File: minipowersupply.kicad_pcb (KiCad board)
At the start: 2 copper layers, 147.4 x 37.3 mm, 107 parts, among them J1 Conn_01x01_Female, J10 Conn_01x03_Female, J11 Conn_01x08_Female, J12 Conn_01x03_Female, J13 Conn_01x08_Female, J14 Conn_01x03_Female, J15 Conn_01x08_Female, J16 Conn_01x02_Female, J17 Conn_01x08_Female, J18 Conn_01x02_Female, J2 Conn_01x03_Male, J3 Conn_01x01_Female, J4 Conn_01x01_Female, J5 Conn_01x03_Male, J6 Conn_01x01_Female, J7 Conn_01x01_Female, J8 Conn_01x03_Male, J9 Conn_01x01_Female, Q1 BC817, U1 ACS70331EOLCTR-2P5U3, U10 ACS70331EOLCTR-2P5U3, U2 ACS70331EOLCTR-2P5U3, U3 ACS70331EOLCTR-2P5U3, U4 CD74HC4067SM, U5 ACS70331EOLCTR-2P5U3, U6 LM7805_TO220, U7 LM317L_TO92, U8 LM337L_TO92, U9 LM358

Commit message: new board with SMD
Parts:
- removed the C10 at (169.0, 123.4)
- removed the C11 at (173.0, 123.4)
- removed the C17 at (165.0, 126.0)
- removed the C18 at (182.4, 133.7)
- removed the C19 at (182.4, 131.2)
- removed the C20 at (186.4, 131.2)
- removed the C21 at (102.4, 57.1)
- removed the C22 at (105.4, 57.1)
- removed the C23 at (115.3, 57.1)
- removed the C26 at (125.2, 57.7)
- removed the C27 at (121.9, 57.7)
- removed C41, C42: 0.1uF, Capacitor_SMD:C_0603_1608Metric
- removed J10, J12, J14: Conn_01x03_Female, Connector_PinHeader_2.54mm:PinHeader_1x03_P2.54mm_Vertical
- removed J11, J13, J15, J17: Conn_01x08_Female, Connector_PinHeader_2.54mm:PinHeader_1x08_P2.54mm_Vertical
- removed the J2 at (101.5, 89.2)
- removed the J5 at (126.2, 89.2)
- removed the J8 at (116.4, 89.2)
- removed the J9 at (112.8, 116.3)
- removed the U5 at (118.2, 102.1)
- removed the U9 at (168.6, 111.3)
- added C15: 0.1uF, Capacitor_SMD:C_0603_1608Metric, F.Cu at (300.6, 79.4)
- added C16: 0.1uF, Capacitor_SMD:C_0603_1608Metric, F.Cu at (300.6, 81.9)
- added C32: 0.1uF, Capacitor_SMD:C_0603_1608Metric, F.Cu at (334.4, 85.8)
- added C33: 0.1uF, Capacitor_SMD:C_0603_1608Metric, F.Cu at (339.3, 79.4)
- added C34: 0.1uF, Capacitor_SMD:C_0603_1608Metric, F.Cu at (338.4, 85.8)
- added J6: Conn_01x01_Female, Connector_PinHeader_2.54mm:PinHeader_1x01_P2.54mm_Vertical, F.Cu at (263.9, 117.3)
- added J7: Conn_01x01_Female, Connector_PinHeader_2.54mm:PinHeader_1x01_P2.54mm_Vertical, F.Cu at (300.9, 93.8)
- added U11: ACS70331EOLCTR-2P5U3, ACS70331EOLCTR-2P5U3:SOIC127P600X175-8N, F.Cu at (333.1, 81.4)
- added U4: LM358, Package_TO_SOT_SMD:SOT-223-8, F.Cu at (293.0, 95.6)
- added U6: LM358, Package_TO_SOT_SMD:SOT-223-8, F.Cu at (293.0, 82.3)
- R19: value 10k -> 20k
- R7: value 20k -> 10k
- moved R20 255.3 mm to (339.3, 81.9)
- moved R19 246.5 mm to (330.4, 85.8)
- moved R2 211.2 mm to (319.7, 81.9), turned to 0 degrees
- moved U1 207.0 mm to (313.5, 81.4), turned to 0 degrees
- moved R1 206.1 mm to (310.8, 85.8)
- moved R4 202.0 mm to (338.0, 94.2), turned to 0 degrees
- moved U2 197.2 mm to (331.8, 93.7), turned to 0 degrees
- moved R3 197.2 mm to (329.1, 98.2)
- moved R6 190.7 mm to (318.4, 95.2), turned to 0 degrees
- moved R7 186.7 mm to (300.6, 86.9)
- moved R5 186.0 mm to (309.5, 99.2)
- moved U3 185.8 mm to (312.2, 94.7), turned to 0 degrees
- moved R8 182.7 mm to (300.6, 84.4), turned to 0 degrees
- moved C5 147.2 mm to (338.0, 91.7)
- moved C2 143.5 mm to (319.7, 79.4)
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- renumbered C12 to C10, C13 to C11, C14 to C12, C15 to C13, C16 to C14, C24 to C17, C25 to C18, C28 to C19, C29 to C20, C30 to C21, C31 to C22, C32 to C23, C33 to C24, C34 to C25, C35 to C26, C36 to C27, C40 to C28, C37 to C29, C38 to C30, C39 to C31, J3 to J2, J4 to J3, J6 to J4, J7 to J5, J16 to J8, J18 to J9, R18 to R16, R16 to R17, R17 to R18, U4 to U5, U6 to U7, U7 to U8, U8 to U9
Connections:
- net +5VA renamed /Clock and TTL/V5Out
- net / Measure and Mux/3v3 renamed 3V3
- net / Measure and Mux/A0 renamed /Filter and Mux/A0
- net / Measure and Mux/A1 renamed /Filter and Mux/A1
- net / Measure and Mux/A2 renamed /Filter and Mux/A2
- net / Measure and Mux/A3 renamed /Filter and Mux/A3
- net / Measure and Mux/Aout renamed /Filter and Mux/Aout
- net / Measure and Mux/Curent and Volt4/Isense renamed /Filter and Mux/Curent and Volt4/Isense
- net / Measure and Mux/Curent and Volt4/Out V renamed /Filter and Mux/Curent and Volt4/Vout
- net / Measure and Mux/Curent and Volt4/Vsense renamed /Filter and Mux/Curent and Volt4/Vsense
- net / Measure and Mux/Curent and Volt5/Isense renamed /Filter and Mux/Curent and Volt5/Isense
- net / Measure and Mux/Curent and Volt5/Out V renamed /Filter and Mux/Curent and Volt5/Vout
- net / Measure and Mux/Curent and Volt6/Isense renamed /Filter and Mux/Curent and Volt6/Isense
- net / Measure and Mux/Curent and Volt6/Out V renamed /Filter and Mux/Curent and Volt6/Vout
- net / Measure and Mux/Curent and Volt6/Vsense renamed /Filter and Mux/Curent and Volt6/Vsense
- net / Measure and Mux/Curent and Volt7/Isense renamed /Filter and Mux/Curent and Volt7/Isense
- net / Measure and Mux/Curent and Volt7/Out V renamed /Filter and Mux/Curent and Volt7/Vout
- net / Measure and Mux/EN renamed /Filter and Mux/EN
- net / Measure and Mux/V5+ renamed V5
- A1 pad 20: unconnected-(A1-Pad20) -> /Clock and TTL/CK_Out
- A1 pad 29: / Measure and Mux/GND -> GNDREF
- A1 pad 30: / Measure and Mux/Vunreg+ -> /Unregulated Power/V+
- A1 pad 4: / Measure and Mux/GND -> GNDREF
- C1 pad 1: / Measure and Mux/GND -> GNDREF
- C10 pad 1: / Measure and Mux/GND -> GNDREF
- C11 pad 1: / Measure and Mux/GND -> GNDREF
- C12 pad 1: / Measure and Mux/GND -> GNDREF
- C13 pad 1: / Measure and Mux/GND -> GNDREF
- C14 pad 1: / Measure and Mux/GND -> GNDREF
- C14 pad 2: / Measure and Mux/Curent and Volt8/Out V -> /Filter and Mux/Curent and Volt8/Vout
- C17 pad 1: /Unregulated Power/GND -> GNDREF
- C18 pad 2: /Unregulated Power/GND -> GNDREF
- C19 pad 1: Net-(C28-Pad1) -> /Unregulated Power/V+
- C19 pad 2: /Clock and TTL/GND_0 -> GNDREF
- C2 pad 2: / Measure and Mux/GND -> GNDREF
- C20 pad 2: /Clock and TTL/GND_0 -> GNDREF
- C21 pad 1: /Clock and TTL/CK -> /Clock and TTL/CK_Out
- C21 pad 2: /Clock and TTL/GND_0 -> GNDREF
- C22 pad 1: Net-(C31-Pad1) -> /Unregulated Power/V+
- C22 pad 2: /DualAdj/GND -> GNDREF
- C23 pad 1: Net-(C32-Pad1) -> /DualAdj/Vreg+
- C23 pad 2: /DualAdj/GND -> GNDREF
- C24 pad 1: Net-(C33-Pad1) -> /Unregulated Power/V-
- C24 pad 2: /DualAdj/GND -> Net-(C24-Pad2)
- C25 pad 1: /DualAdj/GND -> Net-(C24-Pad2)
- C25 pad 2: Net-(C34-Pad2) -> /DualAdj/Vreg-
- C26 pad 1: / Measure and Mux/Curent and Volt7/Vsense -> /Filter and Mux/Curent and Volt5/Vsense
- C26 pad 2: / Measure and Mux/GND -> GNDREF
- C27 pad 1: / Measure and Mux/Unity Inverter1/Ainv -> /Filter and Mux/Unity Inverter/Ainv
- C27 pad 2: / Measure and Mux/GND -> GNDREF
- C28 pad 1: / Measure and Mux/GND -> GNDREF
- C29 pad 1: / Measure and Mux/GND -> GNDREF
- C3 pad 1: / Measure and Mux/Curent and Volt5/Vsense -> /Filter and Mux/Curent and Volt5/Vsense
- C3 pad 2: / Measure and Mux/GND -> GNDREF
- C30 pad 2: / Measure and Mux/GND -> GNDREF
- C31 pad 2: / Measure and Mux/GND -> GNDREF
- C4 pad 1: / Measure and Mux/GND -> GNDREF
- C5 pad 2: / Measure and Mux/GND -> GNDREF
- C6 pad 2: / Measure and Mux/GND -> GNDREF
- C7 pad 1: / Measure and Mux/GND -> GNDREF
- C8 pad 2: / Measure and Mux/GND -> GNDREF
- C9 pad 1: / Measure and Mux/Curent and Volt7/Vsense -> /Filter and Mux/Curent and Volt7/Vsense
- C9 pad 2: / Measure and Mux/GND -> GNDREF
- D1 pad 1: Net-(D1-Pad1) -> /Clock and TTL/HalfSineIn
- D6 pad 1: Net-(D1-Pad1) -> /Clock and TTL/HalfSineIn
- D7 pad 1: /Clock and TTL/GND_0 -> GNDREF
- D8 pad 2: /Clock and TTL/GND_0 -> GNDREF
- D9 pad 1: / Measure and Mux/GND -> GNDREF
- DS1 pad 1: / Measure and Mux/GND -> GNDREF
- DS1 pad 30: / Measure and Mux/GND -> GNDREF
- J5 pad 1: / Measure and Mux/Curent and Volt8/Out V -> /Filter and Mux/Curent and Volt8/Vout
- J8 pad 1: /DualAdj/GND -> GNDREF
- J9 pad 1: /DualAdj/GND -> Net-(C24-Pad2)
- Q1 pad 2: /Clock and TTL/GND_0 -> GNDREF
- Q1 pad 3: /Clock and TTL/CK -> /Clock and TTL/CK_Out
- R1 pad 2: / Measure and Mux/Curent and Volt5/Vsense -> /Filter and Mux/Curent and Volt5/Vsense
- R10 pad 2: Net-(J15-Pad4) -> /Clock and TTL/HalfSineIn
- R11 pad 2: /Clock and TTL/GND_0 -> GNDREF
- R12 pad 1: Net-(C32-Pad1) -> /DualAdj/Vreg+
- R13 pad 1: Net-(C34-Pad2) -> /DualAdj/Vreg-
- R14 pad 2: / Measure and Mux/Unity Inverter1/Ainv -> /Filter and Mux/Unity Inverter/Ainv
- R15 pad 1: / Measure and Mux/Curent and Volt7/Vsense -> /Filter and Mux/Curent and Volt5/Vsense
- R18 pad 2: / Measure and Mux/GND -> GNDREF
- R19 pad 1: Net-(R19-Pad1) -> /Filter and Mux/Curent and Volt8/Vout
- R19 pad 2: / Measure and Mux/Unity Inverter/Ainv -> /Filter and Mux/Curent and Volt8/Vsense
- R2 pad 1: / Measure and Mux/Curent and Volt5/Vsense -> /Filter and Mux/Curent and Volt5/Vsense
- R2 pad 2: / Measure and Mux/GND -> GNDREF
- R20 pad 1: / Measure and Mux/Curent and Volt5/Vsense -> /Filter and Mux/Curent and Volt8/Vsense
- R20 pad 2: Net-(R19-Pad1) -> GNDREF
- R4 pad 2: / Measure and Mux/GND -> GNDREF
- R5 pad 2: / Measure and Mux/Curent and Volt7/Vsense -> /Filter and Mux/Curent and Volt7/Vsense
- R6 pad 1: / Measure and Mux/Curent and Volt7/Vsense -> /Filter and Mux/Curent and Volt7/Vsense
- R6 pad 2: / Measure and Mux/GND -> GNDREF
- R7 pad 1: / Measure and Mux/Curent and Volt8/Out V -> Net-(R7-Pad1)
- R7 pad 2: / Measure and Mux/Curent and Volt8/Vsense -> /Filter and Mux/Unity Inverter1/Ainv
- R8 pad 1: / Measure and Mux/Curent and Volt8/Vsense -> /Filter and Mux/Curent and Volt7/Vsense
- R8 pad 2: / Measure and Mux/GND -> Net-(R7-Pad1)
- R9 pad 2: /Clock and TTL/CK -> /Clock and TTL/CK_Out
- TP3 pad 1: /Unregulated Power/GND -> GNDREF
- TR1 pad 4: /Unregulated Power/GND -> GNDREF
- TR1 pad 5: /Unregulated Power/GND -> GNDREF
- U1 pad 3: / Measure and Mux/Vunreg- -> /Unregulated Power/V-
- U1 pad 4: / Measure and Mux/Vunreg- -> /Unregulated Power/V-
- U1 pad 5: / Measure and Mux/GND -> GNDREF
- U10 pad 3: / Measure and Mux/Vunreg+ -> /Unregulated Power/V+
- U10 pad 4: / Measure and Mux/Vunreg+ -> /Unregulated Power/V+
- U10 pad 5: / Measure and Mux/GND -> GNDREF
- U2 pad 3: / Measure and Mux/Curent and Volt6/Vin -> /DualAdj/Vreg+
- U2 pad 4: / Measure and Mux/Curent and Volt6/Vin -> /DualAdj/Vreg+
- U2 pad 5: / Measure and Mux/GND -> GNDREF
- U3 pad 3: / Measure and Mux/Curent and Volt7/Vin -> /DualAdj/Vreg-
- U3 pad 4: / Measure and Mux/Curent and Volt7/Vin -> /DualAdj/Vreg-
- U3 pad 5: / Measure and Mux/GND -> GNDREF
- U5 pad 12: / Measure and Mux/GND -> GNDREF
- U5 pad 22: / Measure and Mux/Curent and Volt8/Isense -> /Filter and Mux/Curent and Volt8/Isense
- U5 pad 23: / Measure and Mux/Curent and Volt8/Vsense -> /Filter and Mux/Curent and Volt8/Vsense
- U5 pad 3: / Measure and Mux/Unity Inverter1/Ainv -> /Filter and Mux/Unity Inverter1/Ainv
- U5 pad 7: / Measure and Mux/Unity Inverter/Ainv -> /Filter and Mux/Unity Inverter/Ainv
- U7 pad 1: Net-(C28-Pad1) -> /Unregulated Power/V+
- U7 pad 2: /Clock and TTL/GND_0 -> GNDREF
- U8 pad 2: Net-(C32-Pad1) -> /DualAdj/Vreg+
- U8 pad 3: Net-(C31-Pad1) -> /Unregulated Power/V+
- U9 pad 2: Net-(C34-Pad2) -> /DualAdj/Vreg-
- U9 pad 3: Net-(C33-Pad1) -> /Unregulated Power/V-
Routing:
- net /Unregulated Power/V-: track 57.8 -> 21.1 mm
- net /Unregulated Power/V+: track 108.5 -> 73.3 mm
- net /Clock and TTL/CK: track 27.1 -> 0.00 mm
- net /Clock and TTL/V5Out: track 25.6 -> 0.00 mm, vias 1 -> 0
- net Net-(C32-Pad1): track 23.3 -> 0.00 mm
- net Net-(C34-Pad2): track 22.0 -> 0.00 mm
- net Net-(C23-Pad1): track 20.6 -> 0.00 mm
- net Net-(C26-Pad2): track 19.7 -> 0.00 mm
- net Net-(C33-Pad1): track 15.9 -> 0.00 mm
- net Net-(D1-Pad1): track 14.8 -> 0.00 mm, vias 1 -> 0
- net Net-(D7-Pad2): track 13.7 -> 0.00 mm
- net Net-(J11-Pad8): track 11.9 -> 0.00 mm
- net Net-(C27-Pad1): track 11.8 -> 0.00 mm
- net Net-(J9-Pad2): track 11.5 -> 0.00 mm
- net Net-(J8-Pad2): track 8.76 -> 0.00 mm
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- added copper zone on B.Cu, net GNDREF
- added copper zone on F.Cu, net GNDREF
- removed copper zone on B.Cu, net /Clock and TTL/GND_0
- removed copper zone on F.Cu, net /Clock and TTL/GND_0
- removed copper zone on B.Cu, net /DualAdj/GND
- removed copper zone on F.Cu, net /DualAdj/GND
- removed copper zone on B.Cu, net /Unregulated Power/GND
- removed copper zone on F.Cu, net /Unregulated Power/GND
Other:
- board size 147.4 x 37.3 mm -> 126.5 x 129 mm

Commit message: New single board with all SMD in progress
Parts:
- removed U4: LM358, Package_TO_SOT_SMD:SOT-223-8
- C19, C20, U7: moved to F.Cu
- C21, D7, D8, Q1, R10, R11, R12, R15, R7: moved to B.Cu
- C23, C25: footprint Capacitor_SMD:C_1206_3216Metric -> Capacitor_SMD:C_0603_1608Metric
- moved U11 168.0 mm to (165.2, 75.0), turned to -90 degrees
- moved U2 166.7 mm to (165.2, 87.0), turned to -90 degrees
- moved R20 158.2 mm to (181.2, 75.3), turned to 180 degrees
- moved R4 156.6 mm to (181.5, 88.1), turned to 180 degrees
- moved R19 147.1 mm to (183.9, 73.2), turned to -90 degrees
- moved U3 147.0 mm to (165.2, 99.0), turned to -90 degrees
- moved R3 145.7 mm to (183.9, 86.2), turned to -90 degrees
- moved C2 144.7 mm to (175.8, 94.6), turned to 90 degrees
- moved U1 141.8 mm to (172.2, 93.0), turned to -90 degrees
- moved C1 141.7 mm to (173.6, 97.4), turned to 180 degrees
- moved R2 139.2 mm to (181.1, 94.5), turned to 180 degrees
- moved R6 137.4 mm to (181.1, 100.9), turned to 180 degrees
- moved C3 134.8 mm to (184.4, 95.0)
- moved C27 129.2 mm to (167.7, 108.7), turned to -90 degrees
- moved R1 127.4 mm to (183.6, 92.7), turned to -90 degrees
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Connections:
- U6 pad 1: (no net) -> /Filter and Mux/Unity Inverter1/Ainv
- U6 pad 2: (no net) -> Net-(R7-Pad1)
- U6 pad 3: (no net) -> GNDREF
- U6 pad 4: (no net) -> /Unregulated Power/V-
- U6 pad 6: Net-(R7-Pad1) -> Net-(R14-Pad1)
- U6 pad 7: /Filter and Mux/Unity Inverter1/Ainv -> /Filter and Mux/Unity Inverter/Ainv
- U6 pad 8: (no net) -> /Unregulated Power/V+
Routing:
- net /Unregulated Power/V+: track 73.3 -> 115.4 mm
- net Net-(R7-Pad1): vias 0 -> 1
- net Net-(R14-Pad1): vias 0 -> 1
- net /Filter and Mux/Unity Inverter1/Ainv: vias 0 -> 1
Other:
- board size 126.5 x 129 mm -> 102.2 x 63 mm
- board text added: "Safety Cutouts"
- board text added: "VUnreg"
- board text added: "VUnreg-"
- board text added: "Vreg+"

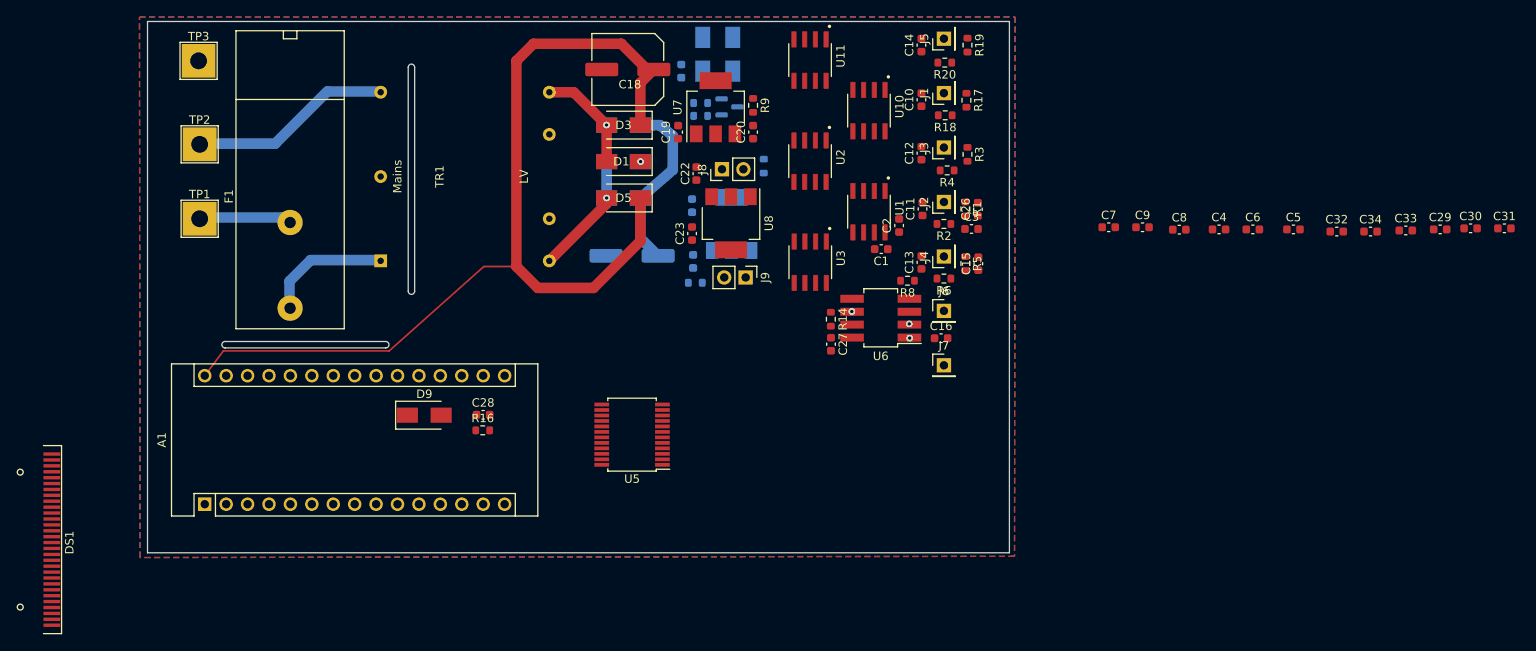
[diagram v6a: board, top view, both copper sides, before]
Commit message: Updated improved board for all SMD
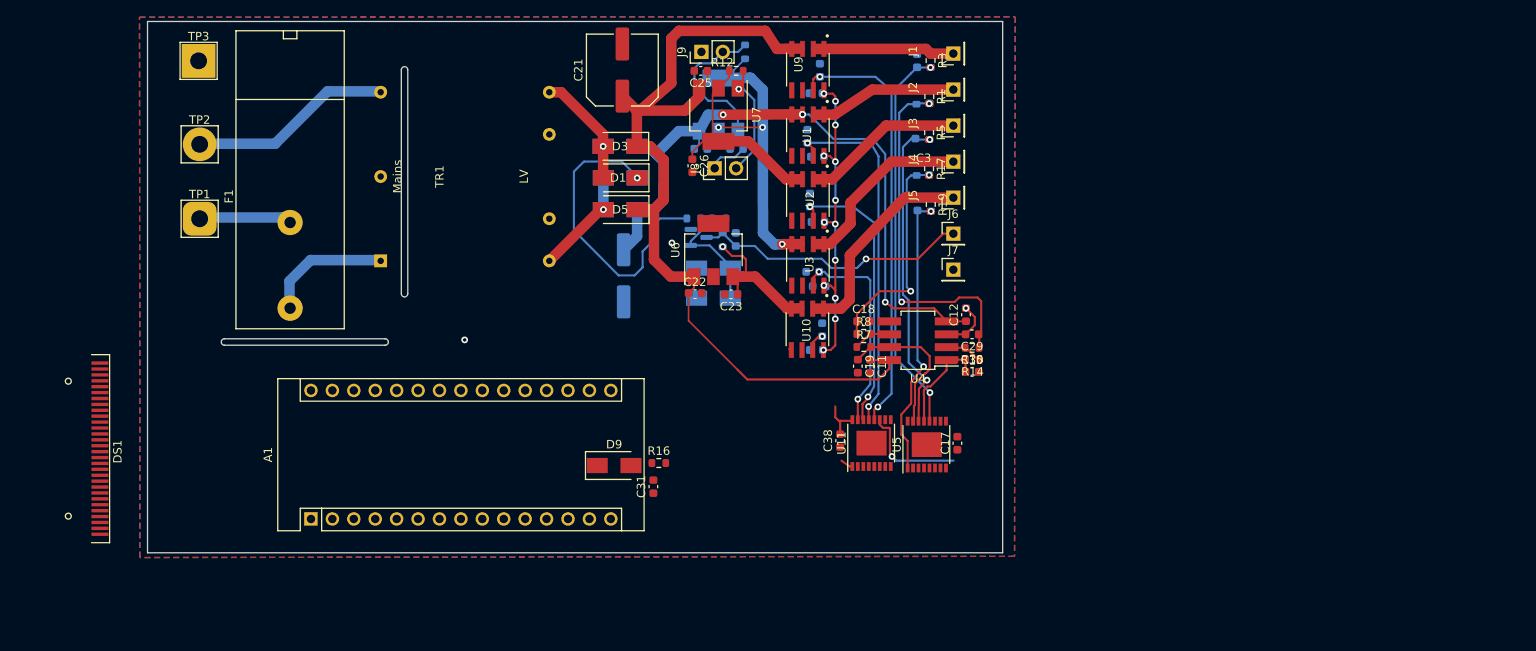
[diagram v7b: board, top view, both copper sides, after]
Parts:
- removed C14, C15, C16, C34: 0.1uF, Capacitor_SMD:C_0603_1608Metric
- added C35: 0.1uF, Capacitor_SMD:C_0603_1608Metric, B.Cu at (166.6, 107.0)
- added C36: 0.1uF, Capacitor_SMD:C_0603_1608Metric, B.Cu at (165.9, 109.4)
- added C38: 0.1uF, Capacitor_SMD:C_0603_1608Metric, F.Cu at (168.8, 120.2)
- added U4: LM358, Package_TO_SOT_SMD:SOT-223-8, F.Cu at (178.0, 108.3)
- A1: value Arduino_Nano_v2.x -> Arduino_Nano_v3.x
- C1, C10, C13, C2, C27, C3, C32, C33, C4, C5, C6, C7, C8, C9, R18, R2, R20, R4, R6, R9: moved to B.Cu
- C17: value 150uF -> 0.1uF; footprint Capacitor_SMD:C_Elec_8x6.2 -> Capacitor_SMD:C_0603_1608Metric; moved to F.Cu
- C18: value 150uF -> 0.1uF; footprint Capacitor_SMD:C_Elec_8x6.2 -> Capacitor_SMD:C_0603_1608Metric
- C20: value 0.1uF -> 150uF; footprint Capacitor_SMD:C_0603_1608Metric -> Capacitor_SMD:C_Elec_8x6.2; moved to B.Cu
- C21: value 0.1uF -> 150uF; footprint Capacitor_SMD:C_0603_1608Metric -> Capacitor_SMD:C_Elec_8x6.2; moved to F.Cu
- C23: value 1uF -> 0.1uF
- C25: value 1uF -> 0.1uF; moved to F.Cu
- C26: value 0.1uF -> 1uF
- C28: value 0.1uF -> 1uF; moved to B.Cu
- R12, R15, R7: moved to F.Cu
- U11: value ACS70331EOLCTR-2P5U3 -> 74HC4051; footprint ACS70331EOLCTR-2P5U3:SOIC127P600X175-8N -> Package_SO:TSSOP-16-1EP_4.4x5mm_P0.65mm
- U5: value CD74HC4067SM -> 74HC4051; footprint Package_SO:SSOP-24_5.3x8.2mm_P0.65mm -> Package_SO:TSSOP-16-1EP_4.4x5mm_P0.65mm
- U6: value LM358 -> LM7805_TO220; footprint Package_TO_SOT_SMD:SOT-223-8 -> Package_TO_SOT_SMD:SOT-223-3_TabPin2
- U7: value LM7805_TO220 -> LM317L_TO92
- U8: value LM317L_TO92 -> LM337L_TO92; moved to B.Cu
- U9: value LM337L_TO92 -> ACS70331EOLCTR-2P5U3; footprint Package_TO_SOT_SMD:SOT-223-3_TabPin2 -> ACS70331EOLCTR-2P5U3:SOIC127P600X175-8N; moved to F.Cu
- moved C31 105.5 mm to (146.6, 125.6), turned to 90 degrees
- moved C33 71.8 mm to (165.9, 79.0), turned to 180 degrees
- moved C32 64.2 mm to (166.4, 76.2), turned to -90 degrees
- moved C30 61.5 mm to (184.4, 112.0)
- moved C29 56.9 mm to (184.4, 107.5), turned to 180 degrees
- moved C5 56.4 mm to (166.2, 94.2), turned to 180 degrees
- moved C4 48.6 mm to (165.2, 91.6), turned to -90 degrees
- moved U11 46.0 mm to (172.5, 120.4), turned to 90 degrees
- moved C6 44.6 mm to (177.9, 75.1), turned to 90 degrees
- moved C17 44.5 mm to (182.7, 120.5), turned to 90 degrees
- moved C28 43.6 mm to (156.5, 85.5), turned to 180 degrees
- moved C8 43.2 mm to (166.3, 101.8), turned to 180 degrees
- moved C18 40.9 mm to (171.5, 106.0), turned to 0 degrees
- moved C7 35.5 mm to (165.5, 100.1)
- moved C19 35.0 mm to (170.9, 111.3), turned to -90 degrees
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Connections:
- A1 pad 10: /Filter and Mux/A3 -> unconnected-(A1-Pad10)
- A1 pad 11: /Filter and Mux/A2 -> /I V Sensor and Mux/A2
- A1 pad 12: /Filter and Mux/A1 -> /I V Sensor and Mux/A1
- A1 pad 13: /Filter and Mux/A0 -> /I V Sensor and Mux/A0
- A1 pad 14: /Filter and Mux/EN -> unconnected-(A1-Pad14)
- A1 pad 20: /Clock and TTL/CK_Out -> /I V Sensor and Mux/Amp
- A1 pad 21: unconnected-(A1-Pad21) -> /Clock and TTL/CK_Out
- A1 pad 30: /Unregulated Power/V+ -> /Clock and TTL/VUnreg+
- C1 pad 2: /Filter and Mux/Curent and Volt5/Isense -> /I V Sensor and Mux/Curent and Volt5/Isense
- C10 pad 1: GNDREF -> /I V Sensor and Mux/Unity Inverter1/Ain
- C10 pad 2: /Filter and Mux/Curent and Volt4/Vout -> GNDREF
- C11 pad 1: GNDREF -> /Clock and TTL/VUnreg+
- C11 pad 2: /Filter and Mux/Curent and Volt5/Vout -> GNDREF
- C12 pad 1: GNDREF -> /DualAdj/VUnreg-
- C12 pad 2: /Filter and Mux/Curent and Volt6/Vout -> GNDREF
- C13 pad 1: GNDREF -> /I V Sensor and Mux/V5+i
- C13 pad 2: /Filter and Mux/Curent and Volt7/Vout -> GNDREF
- C17 pad 2: /Unregulated Power/V- -> V5
- C18 pad 1: /Unregulated Power/V+ -> /I V Sensor and Mux/Unity Inverter1/Ain
- C19 pad 1: /Unregulated Power/V+ -> /I V Sensor and Mux/VA-i
- C20 pad 1: /Clock and TTL/V5Out -> GNDREF
- C20 pad 2: GNDREF -> /DualAdj/VUnreg-
- C21 pad 1: /Clock and TTL/CK_Out -> /Clock and TTL/VUnreg+
- C22 pad 1: /Unregulated Power/V+ -> /Clock and TTL/VUnreg+
- C23 pad 1: /DualAdj/Vreg+ -> /Clock and TTL/V5Out
- C24 pad 1: /Unregulated Power/V- -> /Clock and TTL/CK_Out
- C24 pad 2: Net-(C24-Pad2) -> GNDREF
- C25 pad 1: Net-(C24-Pad2) -> /Clock and TTL/VUnreg+
- C25 pad 2: /DualAdj/Vreg- -> GNDREF
- C26 pad 1: /Filter and Mux/Curent and Volt5/Vsense -> /DualAdj/Vreg+
- C27 pad 1: /Filter and Mux/Unity Inverter/Ainv -> /DualAdj/VUnreg-
- C28 pad 2: Net-(A1-Pad19) -> /DualAdj/Vreg-
- C29 pad 1: GNDREF -> /I V Sensor and Mux/Unity Inverter/Ain
- C29 pad 2: /Filter and Mux/Curent and Volt4/Isense -> GNDREF
- C3 pad 1: /Filter and Mux/Curent and Volt5/Vsense -> /I V Sensor and Mux/Unity Inverter/Ain
- C30 pad 1: 3V3 -> /I V Sensor and Mux/VU-i
- C31 pad 1: /Filter and Mux/Curent and Volt4/Vsense -> GNDREF
- C31 pad 2: GNDREF -> Net-(A1-Pad19)
- C32 pad 2: /Filter and Mux/Curent and Volt8/Isense -> /I V Sensor and Mux/Curent and Volt4/Isense
- C4 pad 2: /Filter and Mux/Curent and Volt6/Isense -> /I V Sensor and Mux/Curent and Volt6/Isense
- C6 pad 1: /Filter and Mux/Curent and Volt6/Vsense -> /I V Sensor and Mux/VU+i
- C7 pad 2: /Filter and Mux/Curent and Volt7/Isense -> /I V Sensor and Mux/Curent and Volt7/Isense
- C9 pad 1: /Filter and Mux/Curent and Volt7/Vsense -> /I V Sensor and Mux/VA+i
- D2 pad 2: /Unregulated Power/V- -> /DualAdj/VUnreg-
- D3 pad 1: /Unregulated Power/V+ -> /Clock and TTL/VUnreg+
- D4 pad 2: /Unregulated Power/V- -> /DualAdj/VUnreg-
- D5 pad 1: /Unregulated Power/V+ -> /Clock and TTL/VUnreg+
- J1 pad 1: /Filter and Mux/Curent and Volt4/Vout -> /I V Sensor and Mux/Curent and Volt4/Vout
- J2 pad 1: /Filter and Mux/Curent and Volt5/Vout -> /I V Sensor and Mux/Curent and Volt5/Vout
- J3 pad 1: /Filter and Mux/Curent and Volt6/Vout -> /I V Sensor and Mux/Curent and Volt6/Vout
- J4 pad 1: /Filter and Mux/Curent and Volt7/Vout -> /I V Sensor and Mux/Curent and Volt7/Vout
- J5 pad 1: /Filter and Mux/Curent and Volt8/Vout -> /I V Sensor and Mux/Curent and Volt8/Vout
- J9 pad 1: Net-(C24-Pad2) -> GNDREF
- R1 pad 1: /Filter and Mux/Curent and Volt5/Vout -> /I V Sensor and Mux/Curent and Volt5/Vout
- R1 pad 2: /Filter and Mux/Curent and Volt5/Vsense -> /I V Sensor and Mux/Unity Inverter/Ain
- R14 pad 2: /Filter and Mux/Unity Inverter/Ainv -> /I V Sensor and Mux/VU-i
- R15 pad 1: /Filter and Mux/Curent and Volt5/Vsense -> /I V Sensor and Mux/Unity Inverter/Ain
- R16 pad 2: /Filter and Mux/Aout -> /I V Sensor and Mux/Volt
- R17 pad 1: /Filter and Mux/Curent and Volt4/Vout -> /I V Sensor and Mux/Curent and Volt7/Vout
- R17 pad 2: /Filter and Mux/Curent and Volt4/Vsense -> /I V Sensor and Mux/Unity Inverter1/Ain
- R18 pad 1: /Filter and Mux/Curent and Volt4/Vsense -> /I V Sensor and Mux/Unity Inverter1/Ain
- R19 pad 1: /Filter and Mux/Curent and Volt8/Vout -> /I V Sensor and Mux/Curent and Volt8/Vout
- R19 pad 2: /Filter and Mux/Curent and Volt8/Vsense -> /I V Sensor and Mux/V5+i
- R2 pad 1: /Filter and Mux/Curent and Volt5/Vsense -> /I V Sensor and Mux/Unity Inverter/Ain
- R20 pad 1: /Filter and Mux/Curent and Volt8/Vsense -> /I V Sensor and Mux/V5+i
- R3 pad 1: /Filter and Mux/Curent and Volt6/Vout -> /I V Sensor and Mux/Curent and Volt4/Vout
- R3 pad 2: /Filter and Mux/Curent and Volt6/Vsense -> /I V Sensor and Mux/VU+i
- R4 pad 1: /Filter and Mux/Curent and Volt6/Vsense -> /I V Sensor and Mux/VU+i
- R5 pad 1: /Filter and Mux/Curent and Volt7/Vout -> /I V Sensor and Mux/Curent and Volt6/Vout
- R5 pad 2: /Filter and Mux/Curent and Volt7/Vsense -> /I V Sensor and Mux/VA+i
- R6 pad 1: /Filter and Mux/Curent and Volt7/Vsense -> /I V Sensor and Mux/VA+i
- R7 pad 2: /Filter and Mux/Unity Inverter1/Ainv -> /I V Sensor and Mux/VA-i
- R8 pad 1: /Filter and Mux/Curent and Volt7/Vsense -> /I V Sensor and Mux/Unity Inverter1/Ain
- U1 pad 1: /Filter and Mux/Curent and Volt5/Vout -> /I V Sensor and Mux/Curent and Volt5/Vout
- U1 pad 2: /Filter and Mux/Curent and Volt5/Vout -> /I V Sensor and Mux/Curent and Volt5/Vout
- U1 pad 3: /Unregulated Power/V- -> /DualAdj/VUnreg-
- U1 pad 4: /Unregulated Power/V- -> /DualAdj/VUnreg-
- U1 pad 7: /Filter and Mux/Curent and Volt5/Isense -> /I V Sensor and Mux/Curent and Volt5/Isense
- U10 pad 1: /Filter and Mux/Curent and Volt4/Vout -> /I V Sensor and Mux/Curent and Volt8/Vout
- U10 pad 2: /Filter and Mux/Curent and Volt4/Vout -> /I V Sensor and Mux/Curent and Volt8/Vout
- U10 pad 3: /Unregulated Power/V+ -> /Clock and TTL/V5Out
- U10 pad 4: /Unregulated Power/V+ -> /Clock and TTL/V5Out
- U10 pad 7: /Filter and Mux/Curent and Volt4/Isense -> /I V Sensor and Mux/Curent and Volt8/Isense
- U11 pad 1: /Filter and Mux/Curent and Volt8/Vout -> /I V Sensor and Mux/Curent and Volt8/Isense
- U11 pad 2: /Filter and Mux/Curent and Volt8/Vout -> unconnected-(U11-Pad2)
- U11 pad 3: /Clock and TTL/V5Out -> /I V Sensor and Mux/Amp
- U11 pad 4: /Clock and TTL/V5Out -> unconnected-(U11-Pad4)
- U11 pad 5: GNDREF -> unconnected-(U11-Pad5)
- U11 pad 7: /Filter and Mux/Curent and Volt8/Isense -> GNDREF
- U11 pad 8: 3V3 -> GNDREF
- U2 pad 1: /Filter and Mux/Curent and Volt6/Vout -> /I V Sensor and Mux/Curent and Volt6/Vout
- U2 pad 2: /Filter and Mux/Curent and Volt6/Vout -> /I V Sensor and Mux/Curent and Volt6/Vout
- U2 pad 7: /Filter and Mux/Curent and Volt6/Isense -> /I V Sensor and Mux/Curent and Volt6/Isense
- U3 pad 1: /Filter and Mux/Curent and Volt7/Vout -> /I V Sensor and Mux/Curent and Volt7/Vout
- U3 pad 2: /Filter and Mux/Curent and Volt7/Vout -> /I V Sensor and Mux/Curent and Volt7/Vout
- U3 pad 7: /Filter and Mux/Curent and Volt7/Isense -> /I V Sensor and Mux/Curent and Volt7/Isense
- U5 pad 1: /Filter and Mux/Aout -> /I V Sensor and Mux/V5+i
- U5 pad 10: /Filter and Mux/A0 -> /I V Sensor and Mux/A1
- U5 pad 11: /Filter and Mux/A1 -> /I V Sensor and Mux/A2
- U5 pad 12: GNDREF -> /I V Sensor and Mux/VU+i
- U5 pad 13: /Filter and Mux/A3 -> /I V Sensor and Mux/VU-i
- U5 pad 14: /Filter and Mux/A2 -> /I V Sensor and Mux/VA+i
- U5 pad 15: /Filter and Mux/EN -> /I V Sensor and Mux/VA-i
- U5 pad 16: unconnected-(U5-Pad16) -> V5
- U5 pad 17: unconnected-(U5-Pad17) -> (no net)
- U5 pad 2: /Filter and Mux/Curent and Volt7/Isense -> unconnected-(U5-Pad2)
- U5 pad 3: /Filter and Mux/Unity Inverter1/Ainv -> /I V Sensor and Mux/Volt
- U5 pad 4: /Filter and Mux/Curent and Volt6/Isense -> unconnected-(U5-Pad4)
- U5 pad 5: /Filter and Mux/Curent and Volt6/Vsense -> unconnected-(U5-Pad5)
- U5 pad 6: /Filter and Mux/Curent and Volt5/Isense -> unconnected-(U5-Pad6)
- U5 pad 7: /Filter and Mux/Unity Inverter/Ainv -> GNDREF
- U5 pad 8: /Filter and Mux/Curent and Volt4/Isense -> GNDREF
- U5 pad 9: /Filter and Mux/Curent and Volt4/Vsense -> /I V Sensor and Mux/A0
- U6 pad 1: /Filter and Mux/Unity Inverter1/Ainv -> /Clock and TTL/VUnreg+
- U6 pad 2: Net-(R7-Pad1) -> GNDREF
- U6 pad 3: GNDREF -> /Clock and TTL/V5Out
- U7 pad 1: /Unregulated Power/V+ -> Net-(J8-Pad2)
- U7 pad 2: GNDREF -> /DualAdj/Vreg+
- U7 pad 3: /Clock and TTL/V5Out -> /Clock and TTL/VUnreg+
- U8 pad 1: Net-(J8-Pad2) -> Net-(J9-Pad2)
- U8 pad 2: /DualAdj/Vreg+ -> /DualAdj/Vreg-
- U8 pad 3: /Unregulated Power/V+ -> /DualAdj/VUnreg-
- U9 pad 1: Net-(J9-Pad2) -> /I V Sensor and Mux/Curent and Volt4/Vout
- U9 pad 2: /DualAdj/Vreg- -> /I V Sensor and Mux/Curent and Volt4/Vout
- U9 pad 3: /Unregulated Power/V- -> /Clock and TTL/VUnreg+
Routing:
- net /Unregulated Power/V+: track 115.4 -> 0.00 mm
- net /Clock and TTL/VUnreg+: track 0.00 -> 105.4 mm
- net /DualAdj/VUnreg-: track 0.00 -> 79.2 mm, vias 0 -> 4
- net /I V Sensor and Mux/Curent and Volt4/Isense: track 0.00 -> 51.3 mm, vias 0 -> 2
- net /I V Sensor and Mux/VU+i: track 0.00 -> 46.4 mm, vias 0 -> 2
- net /I V Sensor and Mux/Curent and Volt5/Isense: track 0.00 -> 43.1 mm, vias 0 -> 2
- net /I V Sensor and Mux/Unity Inverter/Ain: track 0.00 -> 42.2 mm, vias 0 -> 2
- net /DualAdj/Vreg-: track 0.00 -> 39.6 mm, vias 0 -> 3
- net /I V Sensor and Mux/VA+i: track 0.00 -> 37.7 mm, vias 0 -> 2
- net 3V3: track 0.00 -> 37.7 mm, vias 0 -> 13
- net /Clock and TTL/HalfSineIn: track 0.00 -> 36.4 mm
- net /I V Sensor and Mux/Curent and Volt6/Isense: track 0.00 -> 34.1 mm, vias 0 -> 2
- net /I V Sensor and Mux/V5+i: track 0.00 -> 33.8 mm, vias 0 -> 2
- net /Clock and TTL/CK_Out: track 0.00 -> 32.9 mm, vias 0 -> 1
- net /I V Sensor and Mux/Unity Inverter1/Ain: track 0.00 -> 26.2 mm, vias 0 -> 2
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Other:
- board size 102.2 x 63 mm -> 101.4 x 63 mm
- board text added: "5V"
- board text added: "CK"
- board text added: "VA+"
- board text added: "VA-"
- board text added: "VU+"
- board text added: "VU-"
- board text removed: "VUnreg"
- board text removed: "VUnreg-"
- board text removed: "Vreg+"

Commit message: added PDF schematic and images of board to date
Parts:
- C17: moved to B.Cu
- moved A1 10.9 mm to (116.7, 127.0)
- moved C17 8.79 mm to (175.3, 115.7), turned to -90 degrees
- moved C31 6.11 mm to (150.7, 121.1)
- moved D9 5.48 mm to (142.1, 117.6)
- moved R16 5.15 mm to (148.3, 117.8)
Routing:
- net /I V Sensor and Mux/A0: track 0.00 -> 24.0 mm
- net /I V Sensor and Mux/Curent and Volt8/Isense: track 3.86 -> 20.3 mm, vias 1 -> 2
- net /I V Sensor and Mux/A2: track 12.9 -> 25.4 mm, vias 1 -> 2
- net /I V Sensor and Mux/A1: track 0.00 -> 10.9 mm, vias 0 -> 2
- net V5: track 5.14 -> 14.3 mm, vias 0 -> 2
- net GNDREF: vias 3 -> 4
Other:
- board size 101.4 x 63 mm -> 101.4 x 60.4 mm
